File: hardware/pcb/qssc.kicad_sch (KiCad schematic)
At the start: 75 parts, among them J1 FT232RL, J10 USB-C, J2 5V Barrel, J3 SMA, J4 Emitter drv, J5 Detector FE, J6 DET_BIAS, J7 RESET, J8 MW_GATE, J9 JTAG, U1 XC7A35T-1CPG236C, U3 ADF4351BCPZ, U5 HMC441LP3E, U7 ADA4530-1, Y1 100MHz TCXO

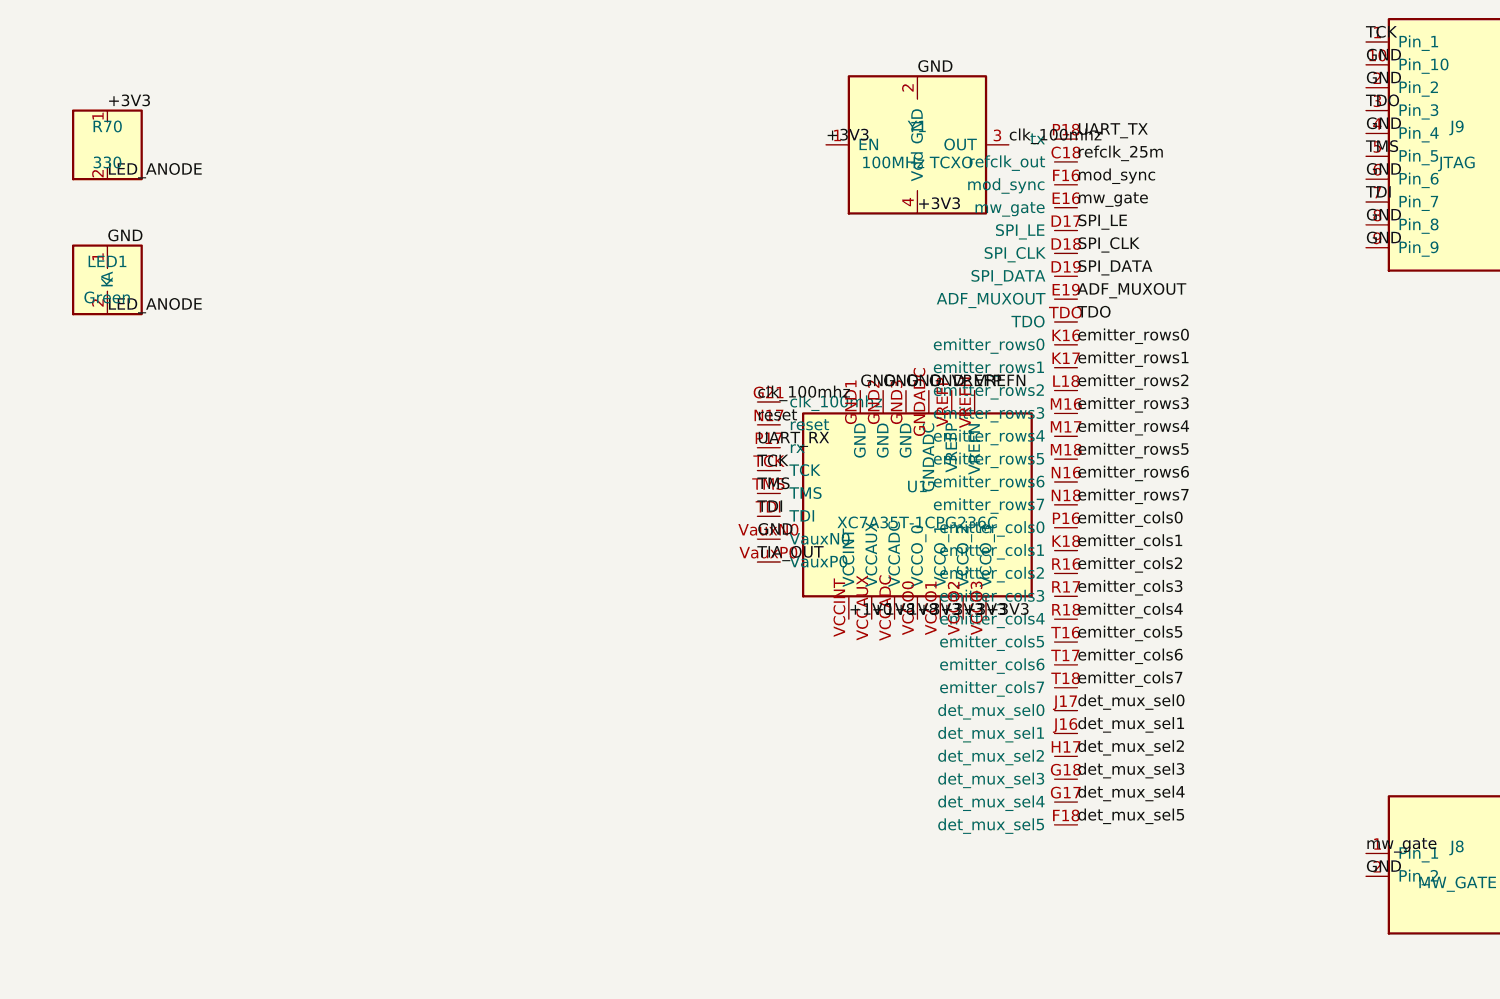
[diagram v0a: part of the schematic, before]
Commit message: pcb: fix FPGA GND-ball netting (52 balls were wrongly +3V3) + full CPG236 ball map
The FPGA power/ground net map was missing the "GND" key in _FPGA_PWR_NET,
so all 52 GND balls fell through the `else "+3V3"` branch (intended only for
VCCO_* banks) and were netted +3V3 — electrically wrong though DRC appeared
clean (all pads on the same wrong net, no conflict).

Fix: add "GND":"GD" to _FPGA_PWR_NET. Now A1/W1/... -> GND as datasheet
intended.

Verified:
  fpga_net_map(): A1->GND, W1->GND, GND=67 balls, +3V3=30, +1V0=8, +1V8=3
  saved PCB sexp: 157 pads netted (67 GND/30 +3V3/8 +1V0/3 +1V8), 81 NC spare-IO
  kicad-cli pcb drc: 0 violations, 0 unconnected, 0 footprint errors

Co-Authored-By: Claude <noreply@anthropic.com>
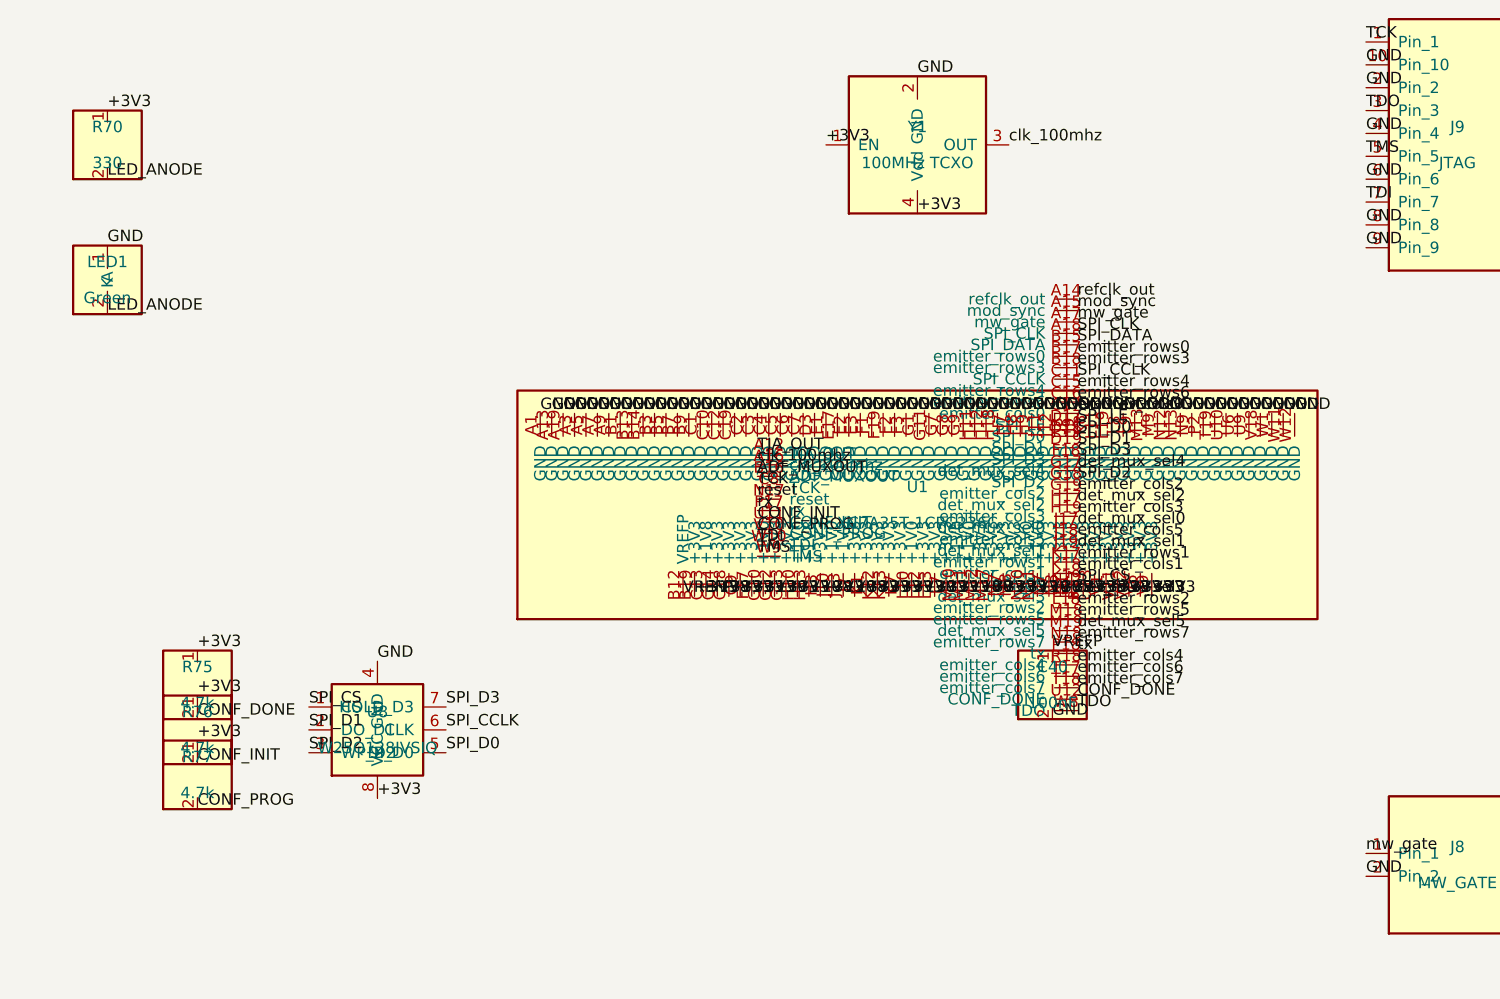
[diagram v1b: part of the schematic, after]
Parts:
- added C40: 100nF, Capacitor_SMD:C_0603_1608Metric, symbol qssc:C
- added R75, R76, R77: 4.7k, Resistor_SMD:R_0603_1608Metric, symbol qssc:R
- added U8: W25Q128JVSIQ, Package_SO:SOIC-8_3.9x4.9mm_P1.27mm, symbol qssc:W25Q128JVS
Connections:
- net +1V0: now also U1.G10 (+1V0), U1.H10 (+1V0), U1.J10 (+1V0), U1.L10 (+1V0), U1.M10 (+1V0), U1.M11 (+1V0), U1.N10 (+1V0), U1.N11 (+1V0); no longer U1.VCCINT
- net +1V8: now also U1.C13 (+1V8), U1.H13 (+1V8), U1.J13 (+1V8); no longer U1.VCCADC, U1.VCCAUX
- net +3V3: now also U1.B19 (+3V3), U1.C14 (+3V3), U1.C18 (+3V3), U1.C9 (+3V3), U1.F17 (+3V3), U1.G12 (+3V3), U1.G13 (+3V3), U1.H3 (+3V3), U1.J7 (+3V3), U1.K1 (+3V3), U1.K12 (+3V3), U1.K13 (+3V3), U1.K7 (+3V3), U1.L12 (+3V3), U1.L13 (+3V3), U1.L7 (+3V3), U1.M12 (+3V3), U1.M17 (+3V3), U1.M7 (+3V3), U1.M8 (+3V3), U1.N7 (+3V3), U1.N8 (+3V3), U1.R1 (+3V3), U1.R17 (+3V3), U1.U13 (+3V3), U1.V1 (+3V3), U1.V11 (+3V3), U1.V12 (+3V3), U1.V6 (+3V3), U1.V9 (+3V3), R75.1, R76.1, R77.1, U8.8 (VCC); no longer U1.VCCO0 (VCCO_0), U1.VCCO1 (VCCO_1), U1.VCCO2 (VCCO_2), U1.VCCO3 (VCCO_3)
- net ADF_MUXOUT: now also U1.B16 (ADF_MUXOUT); no longer U1.E19 (ADF_MUXOUT)
- net GND: now also J4.9 (Pin_9), U1.A1 (GND), U1.A13 (GND), U1.A19 (GND), U1.A3 (GND), U1.A5 (GND), U1.A7 (GND), U1.A9 (GND), U1.B1 (GND), U1.B13 (GND), U1.B14 (GND), U1.B3 (GND), U1.B5 (GND), U1.B7 (GND), U1.B9 (GND), U1.C1 (GND), U1.C10 (GND), U1.C12 (GND), U1.C17 (emitter_cols0), U1.C19 (GND), U1.C2 (GND), U1.C3 (GND), U1.C4 (GND), U1.C5 (GND), U1.C6 (GND), U1.C7 (GND), U1.D3 (GND), U1.E1 (GND), U1.E17 (GND), U1.E2 (GND), U1.E3 (GND), U1.F1 (GND), U1.F19 (GND), U1.F2 (GND), U1.F3 (GND), U1.G1 (GND), U1.G11 (GND), U1.G7 (GND), U1.G8 (GND), U1.G9 (GND), U1.H11 (GND), U1.H12 (GND), U1.H18 (GND), U1.H7 (GND), U1.H8 (GND), U1.H9 (GND), U1.J11 (GND), U1.J12 (GND), U1.J8 (GND), U1.J9 (GND), U1.K8 (GND), U1.L11 (GND), U1.L19 (GND), U1.L8 (GND), U1.L9 (GND), U1.M13 (GND), U1.M9 (GND), U1.N12 (GND), U1.N13 (GND), U1.N9 (GND), U1.P2 (GND), U1.T19 (GND), U1.U10 (GND), U1.U6 (GND), U1.U9 (GND), U1.V18 (GND), U1.W1 (GND), U1.W11 (GND), U1.W12 (GND), C40.2, U8.4 (GND); no longer U1.GND1 (GND), U1.GND2 (GND), U1.GND3 (GND), U1.GNDADC, U1.VauxN0
- net SPI_CLK: now also U1.A18 (SPI_CLK); no longer U1.D18 (SPI_CLK)
- net SPI_DATA: now also U1.B15 (SPI_DATA); no longer U1.D19 (SPI_DATA)
- net TCK: now also U1.C8 (TCK); no longer U1.TCK
- net TDI: now also U1.W10 (TDI); no longer U1.TDI
- net TDO: now also U1.W8 (TDO); no longer U1.TDO
- net TIA_OUT: now also U1.A12 (TIA_OUT); no longer U1.VauxP0
- net TMS: now also U1.W9 (TMS); no longer U1.TMS
- net UART_RX: no longer U1.P17 (rx)
- net UART_TX: no longer U1.P18 (tx)
- net VREFP: now also U1.B12 (VREFP), C40.1; no longer U1.VREFP
- net clk_100mhz: now also U1.A16 (clk_100mhz); no longer U1.G21 (clk_100mhz)
- net det_mux_sel1: now also U1.J19 (det_mux_sel1); no longer U1.J16 (det_mux_sel1)
- net det_mux_sel3: now also U1.L17 (det_mux_sel3); no longer U1.G18 (det_mux_sel3)
- net det_mux_sel5: now also U1.M19 (det_mux_sel5); no longer U1.F18 (det_mux_sel5)
- net emitter_cols2: now also U1.G19 (emitter_cols2); no longer U1.R16 (emitter_cols2)
- net emitter_cols3: now also U1.H19 (emitter_cols3); no longer U1.R17 (emitter_cols3)
- net emitter_cols5: now also U1.J18 (emitter_cols5); no longer U1.T16 (emitter_cols5)
- net emitter_rows0: now also U1.B17 (emitter_rows0); no longer U1.K16 (emitter_rows0)
- net emitter_rows3: now also U1.B18 (emitter_rows3); no longer U1.M16 (emitter_rows3)
- net emitter_rows4: now also U1.C15 (emitter_rows4); no longer U1.M17 (emitter_rows4)
- net emitter_rows6: now also U1.C16 (emitter_rows6); no longer U1.N16 (emitter_rows6)
- net mod_sync: now also U1.A15 (mod_sync); no longer U1.F16 (mod_sync)
- net mw_gate: now also U1.A17 (mw_gate); no longer U1.E16 (mw_gate)
- net refclk_25m: no longer U1.C18 (refclk_out)
- removed net VREFN: U1.VREFN
- removed net emitter_cols0: J4.9 (Pin_9), U1.P16 (emitter_cols0)
- new net CONF_DONE: R75.2, U1.U12 (CONF_DONE)
- new net CONF_INIT: R76.2, U1.U11 (CONF_INIT)
- new net CONF_PROG: R77.2, U1.V10 (CONF_PROG)
- new net SPI_CCLK: U1.C11 (SPI_CCLK), U8.6 (CLK)
- new net SPI_CS: U1.K19 (SPI_CS), U8.1 (CS)
- new net SPI_D0: U1.D18 (SPI_D0), U8.5 (DI_D0)
- new net SPI_D1: U1.D19 (SPI_D1), U8.2 (DO_D1)
- new net SPI_D2: U1.G18 (SPI_D2), U8.3 (WP_D2)
- new net SPI_D3: U1.F18 (SPI_D3), U8.7 (HOLD_D3)
- new net refclk_out: U1.A14 (refclk_out)
- new net rx: U1.P17 (rx)
- new net tx: U1.P18 (tx)

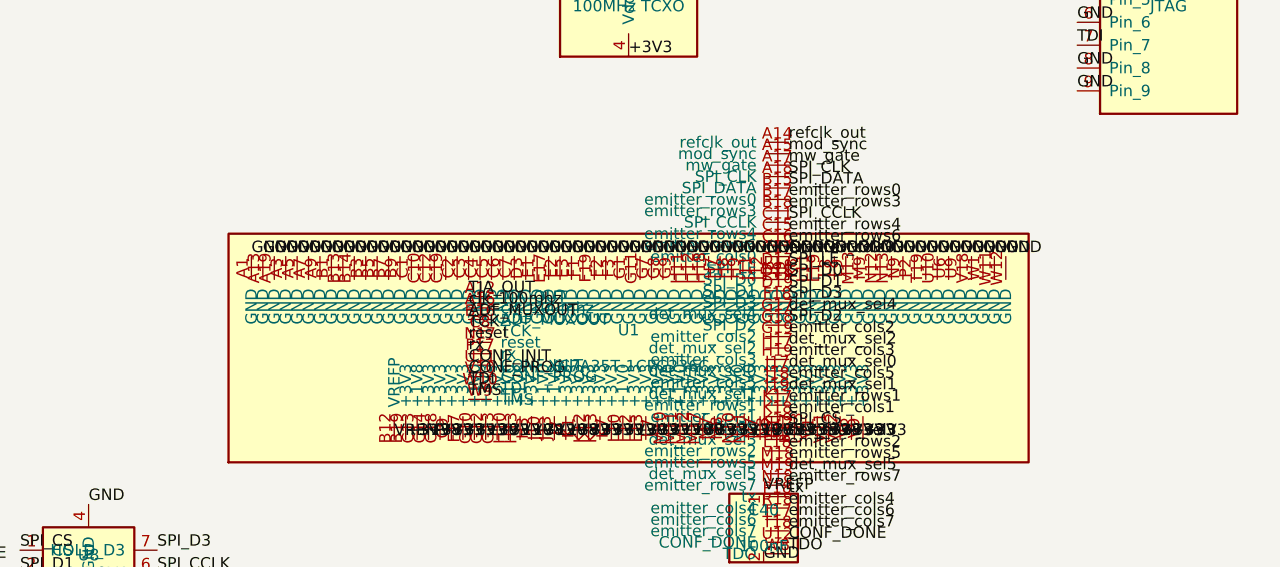
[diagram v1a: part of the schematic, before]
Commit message: fpga: ground all 22 MGT_GND balls + reproducible CPG236 ball-map generator
The hand-built ball map grounded only 10 of the 22 MGT_GND balls (A2,A4,
A6,A8,A10,B2,B4,B6,B8,B10,D1,D2 were left floating). DRC was clean because
unnetted BGA pads aren't flagged -- but per UG475 every MGT_GND pad on the
CPG236 package must tie to ground even though XC7A35T has no MGT transceiver.

Add tools/gen_fpga_ballmap.py: parses the real FPGA_Xilinx_Artix7:
XC7A35T-CPG236 symbol (238 pads) and emits .tmpwork/fpga_cpg236_map.json,
deriving the power dict authoritatively from pin names so a ground/supply
ball can never be silently dropped. signals/config/jtag/xadc sections are
design choices preserved (all verified on real IO / dedicated pins; clk
on A16 = IO_L12P_T1_MRCC_16, a clock-capable pin).

Verified after regen:
  238 pads total, 168 netted, 70 NC (68 spare IO + DXP/DXN temp diode)
  GND=79 (52 GND + 22 MGT_GND + GNDADC + VREFN + VN + M1 + M2)
  A2/A10 -> GND (were floating); A12 -> TIA_OUT; A16 -> clk_100mhz
  kicad-cli pcb drc: 0 violations, 0 unconnected

Co-Authored-By: Claude <noreply@anthropic.com>
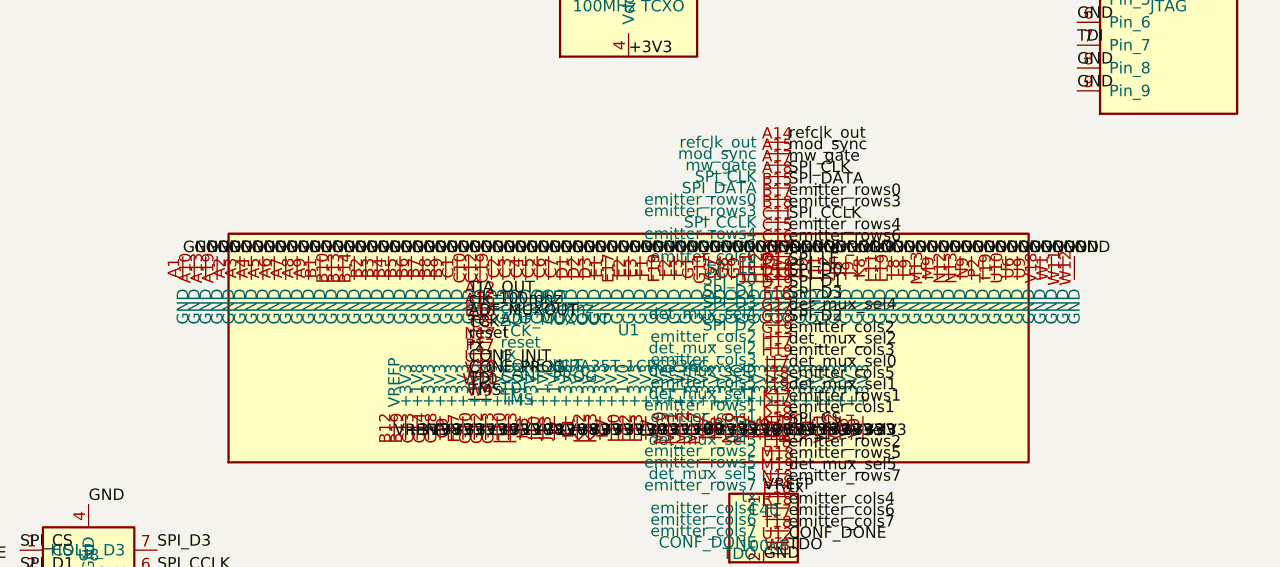
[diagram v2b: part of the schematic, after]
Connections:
- net GND: now also U1.A10 (GND), U1.A2 (GND), U1.A4 (GND), U1.A6 (GND), U1.A8 (GND), U1.B10 (GND), U1.B2 (GND), U1.B4 (GND), U1.B6 (GND), U1.B8 (GND), U1.D1 (GND), U1.D2 (GND)

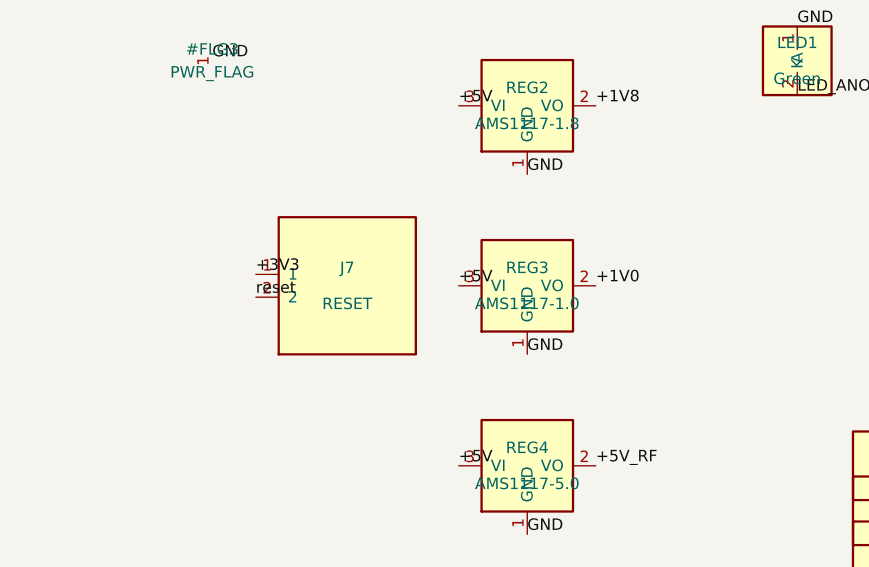
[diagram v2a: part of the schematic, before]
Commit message: pcb: replace fake AMS1117-1.0 with real AP2127K-1.0 + VREFP PWR_FLAG
AMS1117 has no 1.0 V option (min fixed output 1.5 V), so the VCCINT=1.0 V
rail's "AMS1117-1.0" was a non-existent part. Use the AP2127K-1.0 (Diodes
Inc, 600 mA, SOT-23-5) with its datasheet pinout (1=VIN 2=GND 3=EN 4=BP
5=VOUT): VIN/EN tied to +5V, BP decoupled via C41 10nF, VOUT->+1V0 with
10uF/100nF local decoupling (C43/C44) and a 10uF input cap (C42).

Also fix a pre-existing ERC error: U1 pin B12 (VREFP, power input) was
not driven -- the Artix-7 XADC internal 1.25 V reference drives VREFP but
ERC cannot see it. Add #FLG4 PWR_FLAG on VREFP.

Verified:
  kicad-cli sch erc: 0 errors / 145 warnings (all endpoint_off_grid, benign)
  kicad-cli pcb drc: 0 violations / 0 unconnected / 0 footprint errors
  REG3 pads netted: 1->+5V 2->GND 3->+5V 4->BP_1V0 5->+1V0 (datasheet pinout)
  +1V0 rail: 17 pins (REG3 VOUT + 8x FPGA VCCINT + bulk/decoupling/ESD)
  ruff clean; 88 components (was 75)

Co-Authored-By: Claude <noreply@anthropic.com>
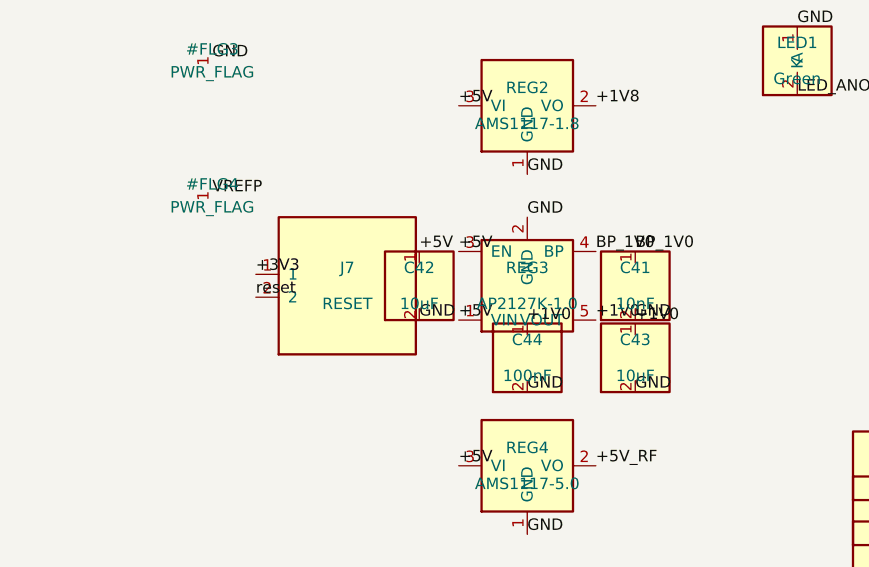
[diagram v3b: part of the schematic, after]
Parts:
- removed REG3: AMS1117-1.0, Package_TO_SOT_SMD:SOT-223-3_TabPin2, symbol qssc:AMS1117-1.0
- added C41: 10nF, Capacitor_SMD:C_0603_1608Metric, symbol qssc:C
- added C42, C43: 10uF, Capacitor_SMD:C_0805_2012Metric, symbol qssc:C
- added C44: 100nF, Capacitor_SMD:C_0603_1608Metric, symbol qssc:C
- added REG3: AP2127K-1.0, Package_TO_SOT_SMD:SOT-23-5, symbol qssc:AP2127K-1.0
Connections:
- net +1V0: now also C43.1, C44.1, REG3.5 (VOUT)
- net +5V: now also C42.1, REG3.1 (VIN), REG3.3 (EN)
- net GND: now also C41.2, C42.2, C43.2, C44.2, REG3.2 (GND)
- new net BP_1V0: C41.1, REG3.4 (BP)
